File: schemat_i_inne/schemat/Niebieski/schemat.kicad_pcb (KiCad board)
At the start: 2 copper layers, 260.4 x 151.1 mm, 23 parts, among them J1 Hole1, J2 Hole2, J3 Hole3, J4 Hole4, J5 RJ45, SW1 SW_DIP_x01, SW2 Left, SW3 Up, SW4 Down, SW5 Right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

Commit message: Good footprints, before changes on PCB
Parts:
- added C3: 100N, Connector_PinHeader_2.54mm:PinHeader_1x02_P2.54mm_Vertical, F.Cu at (251.0, 105.7)
- added C4: 2.2uF, Connector_PinHeader_2.54mm:PinHeader_1x02_P2.54mm_Vertical, F.Cu at (281.6, 70.4)
- added R1: 4K7, Resistor_SMD:R_0805_2012Metric_Pad1.20x1.40mm_HandSolder, F.Cu at (255.7, 104.8)
- added R2: 1K, Resistor_SMD:R_0805_2012Metric_Pad1.20x1.40mm_HandSolder, F.Cu at (286.3, 72.5)
- added R3: 1K, Resistor_SMD:R_0805_2012Metric_Pad1.20x1.40mm_HandSolder, F.Cu at (281.7, 76.7)
- added R4: 1K, Resistor_SMD:R_0805_2012Metric_Pad1.20x1.40mm_HandSolder, F.Cu at (286.3, 69.5)
- added U4: LF33_TO252, Package_TO_SOT_SMD:TO-252-2, F.Cu at (285.4, 64.0)
- added U5: SN74LS07, Package_DIP:DIP-14_W7.62mm_LongPads, F.Cu at (298.2, 63.5)
- added U6: SD, Connector_Card:SD_Kyocera_145638009511859+, F.Cu at (263.5, 74.3)
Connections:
- C2 pad 1: VCC -> +5V
- J1 pad 1: Net-(J1-Pad1) -> unconnected-(J1-Pad1)
- J2 pad 1: Net-(J2-Pad1) -> unconnected-(J2-Pad1)
- J3 pad 1: Net-(J3-Pad1) -> unconnected-(J3-Pad1)
- J4 pad 1: Net-(J4-Pad1) -> unconnected-(J4-Pad1)
- J5 pad 1: VCC -> +5V
- J5 pad 3: Net-(J5-Pad3) -> unconnected-(J5-Pad3)
- J5 pad 6: Net-(J5-Pad6) -> /SCK
- J5 pad 7: Net-(J5-Pad7) -> /MISO
- J5 pad 8: Net-(J5-Pad8) -> /MOSI
- RV1 pad 3: VCC -> +5V
- U1 pad 1: Net-(J5-Pad8) -> /MOSI
- U1 pad 10: Net-(U1-Pad10) -> unconnected-(U1-Pad10)
- U1 pad 17: VCC -> +5V
- U1 pad 2: Net-(J5-Pad7) -> /MISO
- U1 pad 27: VCC -> +5V
- U1 pad 29: Net-(U1-Pad29) -> unconnected-(U1-Pad29)
- U1 pad 3: Net-(J5-Pad6) -> /SCK
- U1 pad 30: Net-(U1-Pad30) -> unconnected-(U1-Pad30)
- U1 pad 31: Net-(U1-Pad31) -> unconnected-(U1-Pad31)
- U1 pad 32: Net-(U1-Pad32) -> unconnected-(U1-Pad32)
- U1 pad 33: Net-(U1-Pad33) -> unconnected-(U1-Pad33)
- U1 pad 37: Net-(R1-Pad2) -> /CS
- U1 pad 38: VCC -> +5V
- U1 pad 40: Net-(U1-Pad40) -> unconnected-(U1-Pad40)
- U1 pad 5: VCC -> +5V
- U1 pad 9: Net-(U1-Pad9) -> unconnected-(U1-Pad9)
- U2 pad 3: VCC -> +5V
- U3 pad 17: VCC -> +5V
- U3 pad 19: VCC -> +5V
- U3 pad 4: VCC -> +5V
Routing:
- net +5V: track 0.00 -> 357.9 mm
- net VCC: track 357.9 -> 0.00 mm
- net Net-(J5-Pad7): track 146.5 -> 0.00 mm
- net /MISO: track 0.00 -> 146.5 mm
- net Net-(J5-Pad6): track 133.7 -> 0.00 mm
- net /SCK: track 0.00 -> 133.7 mm
- net Net-(J5-Pad8): track 132.3 -> 0.00 mm
- net /MOSI: track 0.00 -> 132.3 mm
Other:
- net class Default removed

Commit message: Wstepne sciezki z buforem
-> Dodano wstepne sciezki razem z buforem
-> Tam gdzie bylo to wymagane zmieniono warstwe
-> Dodano oporniki 0R we wlasciwych miejscach
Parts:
- added R5: 0R, Resistor_THT:R_Axial_DIN0207_L6.3mm_D2.5mm_P10.16mm_Horizontal, F.Cu at (252.0, 160.0)
- added R6: 0R, Resistor_THT:R_Axial_DIN0207_L6.3mm_D2.5mm_P10.16mm_Horizontal, F.Cu at (259.1, 144.8)
- C3, C4, U5: moved to B.Cu
- moved U4 88.5 mm to (285.0, 152.6), turned to 90 degrees
- moved C4 83.9 mm to (291.6, 153.7)
- moved U5 75.7 mm to (272.3, 134.6), turned to -90 degrees
- moved R2 62.2 mm to (266.7, 131.6), turned to -90 degrees
- moved R4 61.0 mm to (287.5, 130.6), turned to 180 degrees
- moved C3 57.1 mm to (278.9, 155.5)
- moved R3 54.2 mm to (269.2, 129.5), turned to -90 degrees
- moved R1 49.6 mm to (285.0, 144.8)
- moved U6 45.0 mm to (281.9, 115.3), turned to 180 degrees
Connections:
- C3 pad 1: +5V -> Net-(R1-Pad1)
- R1 pad 1: +5V -> Net-(R1-Pad1)
- U4 pad 1: +5V -> Net-(R1-Pad1)
- U5 pad 1: /CS -> Net-(U5-Pad1)
- U5 pad 14: +5V -> Net-(R1-Pad1)
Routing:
- net GND: track 858.1 -> 952.8 mm
- net +3V3: track 0.00 -> 71.9 mm
- net /MISO: track 146.5 -> 187.5 mm
- net /SCK: track 133.7 -> 169.1 mm
- net Net-(R1-Pad1): track 8.64 -> 41.7 mm
- net /MOSI: track 132.3 -> 164.2 mm
- net Net-(U5-Pad1): track 0.00 -> 29.2 mm
- net Net-(U5-Pad9): track 0.00 -> 25.0 mm
- net Net-(R3-Pad2): track 0.00 -> 19.2 mm
- net Net-(R2-Pad2): track 0.00 -> 16.1 mm
- net Net-(R4-Pad2): track 0.00 -> 11.0 mm
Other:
- board outline removed

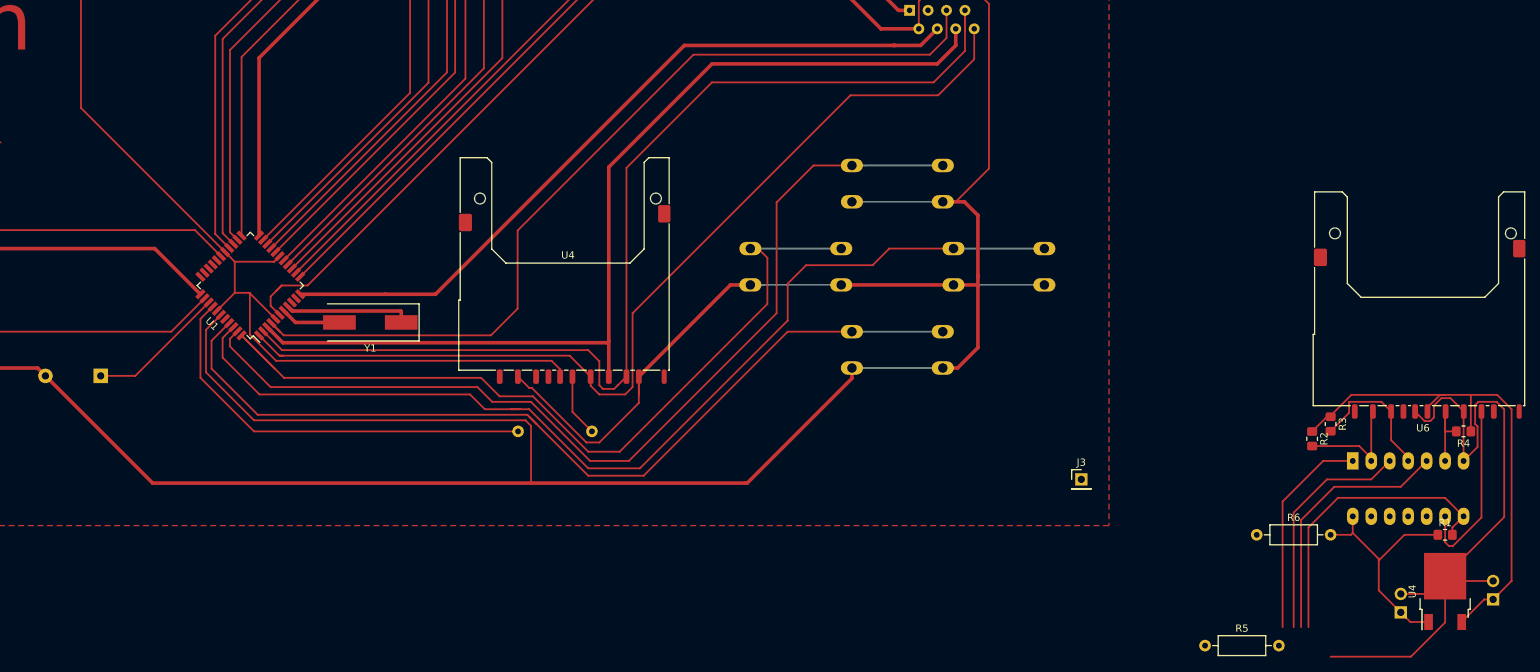
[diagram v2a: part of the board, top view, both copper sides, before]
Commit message: Awful but should work v2
-> Wszystko zostalo prowizorycznie podlaczone
-> uzyto 3 opornikow 0R
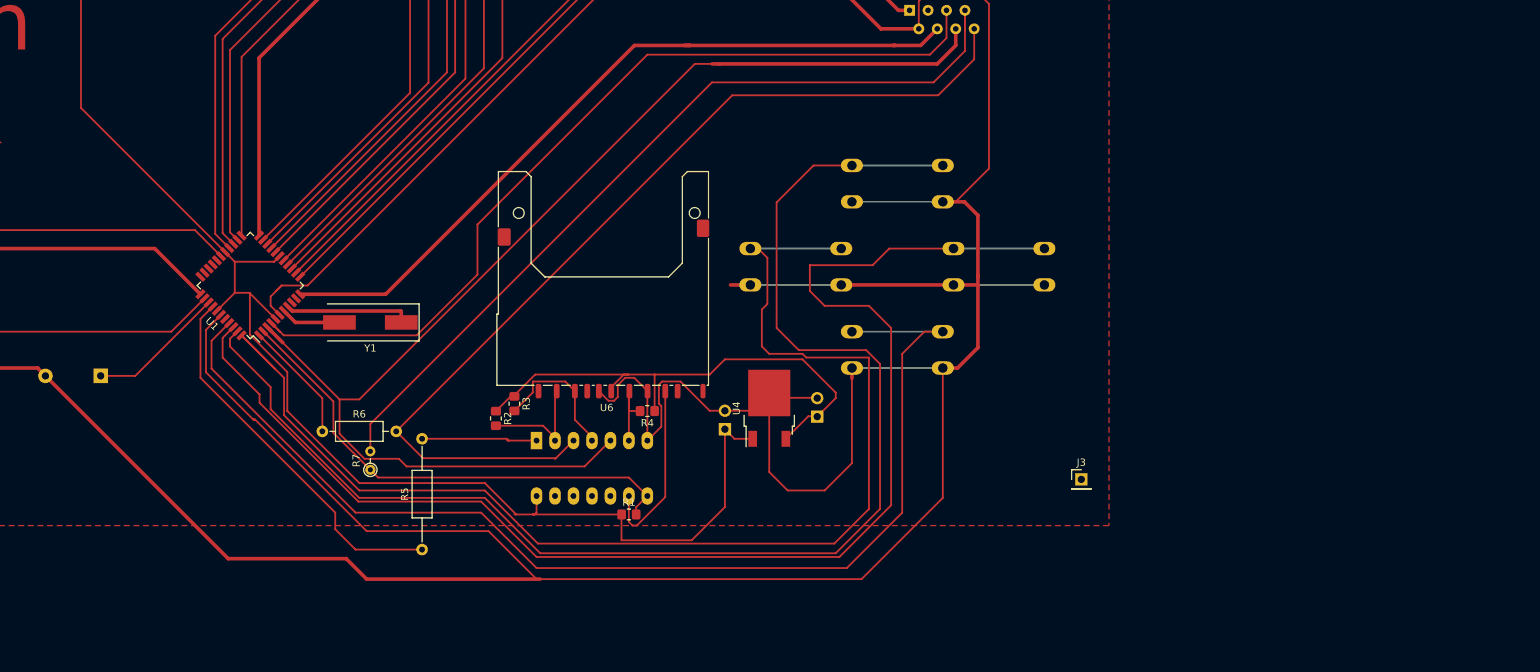
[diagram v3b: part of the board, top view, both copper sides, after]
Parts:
- removed the R1 at (167.6, 130.6)
- removed the U4 at (164.3, 115.8)
- added R7: 0R, Resistor_THT:R_Axial_DIN0204_L3.6mm_D1.6mm_P2.54mm_Vertical, F.Cu at (137.2, 135.8)
- R5: footprint Resistor_THT:R_Axial_DIN0207_L6.3mm_D2.5mm_P10.16mm_Horizontal -> Resistor_THT:R_Axial_DIN0207_L6.3mm_D2.5mm_P15.24mm_Horizontal
- moved R6 129.3 mm to (130.6, 130.6)
- moved R4 112.3 mm to (175.3, 127.8)
- moved R1 112.3 mm to (172.7, 142.0)
- moved R2 112.3 mm to (154.4, 128.8)
- moved R3 112.3 mm to (157.0, 126.7)
- moved U5 112.3 mm to (160.0, 131.8)
- moved U6 112.3 mm to (169.7, 112.5)
- moved R5 108.5 mm to (144.3, 146.8), turned to 90 degrees
- moved C3 96.3 mm to (185.9, 130.3)
- moved U4 96.3 mm to (192.0, 127.4)
- moved C4 96.3 mm to (198.6, 128.5)
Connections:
- C3 pad 1: Net-(R1-Pad1) -> +5V
- J5 pad 7: /MISO -> Net-(J5-Pad7)
- J5 pad 8: /MOSI -> Net-(U5-Pad3)
- R1 pad 1: Net-(R1-Pad1) -> +5V
- R6 pad 1: +5V -> /MOSI
- R6 pad 2: Net-(R1-Pad1) -> Net-(U5-Pad3)
- U4 pad 1: Net-(R1-Pad1) -> +5V
- U5 pad 14: Net-(R1-Pad1) -> +5V
- U5 pad 3: /MOSI -> Net-(U5-Pad3)
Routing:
- net /MOSI: track 164.2 -> 16.9 mm
- net Net-(U5-Pad3): track 0.00 -> 132.2 mm
- net /MISO: track 187.5 -> 67.9 mm
- net Net-(J5-Pad7): track 0.00 -> 115.5 mm
- net GND: track 952.8 -> 855.4 mm
- net Net-(SW2-Pad1): track 115.5 -> 173.7 mm
- net Net-(R1-Pad2): track 57.9 -> 0.00 mm
- net +5V: track 357.9 -> 414.7 mm
- net Net-(SW3-Pad1): track 132.8 -> 186.5 mm
- net /CS: track 0.00 -> 52.8 mm
- net Net-(SW5-Pad1): track 140.6 -> 186.1 mm
- net Net-(R1-Pad1): track 41.7 -> 0.00 mm
- net Net-(SW4-Pad1): track 123.6 -> 158.0 mm
- net Net-(R5-Pad2): track 29.2 -> 16.1 mm
- net Net-(J5-Pad5): track 122.6 -> 120.4 mm
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
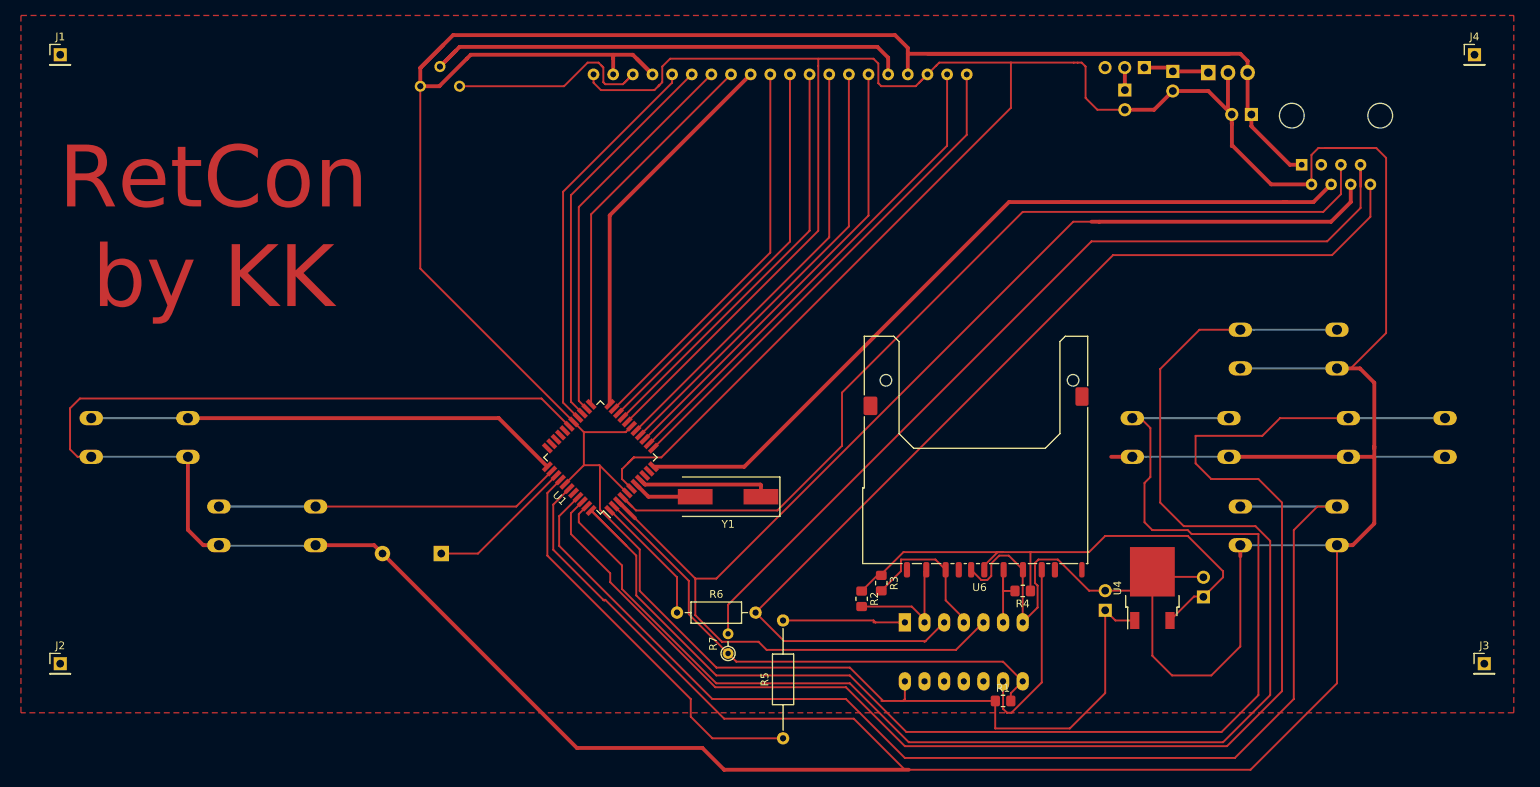
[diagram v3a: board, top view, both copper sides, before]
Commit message: Not all connections, but better positions
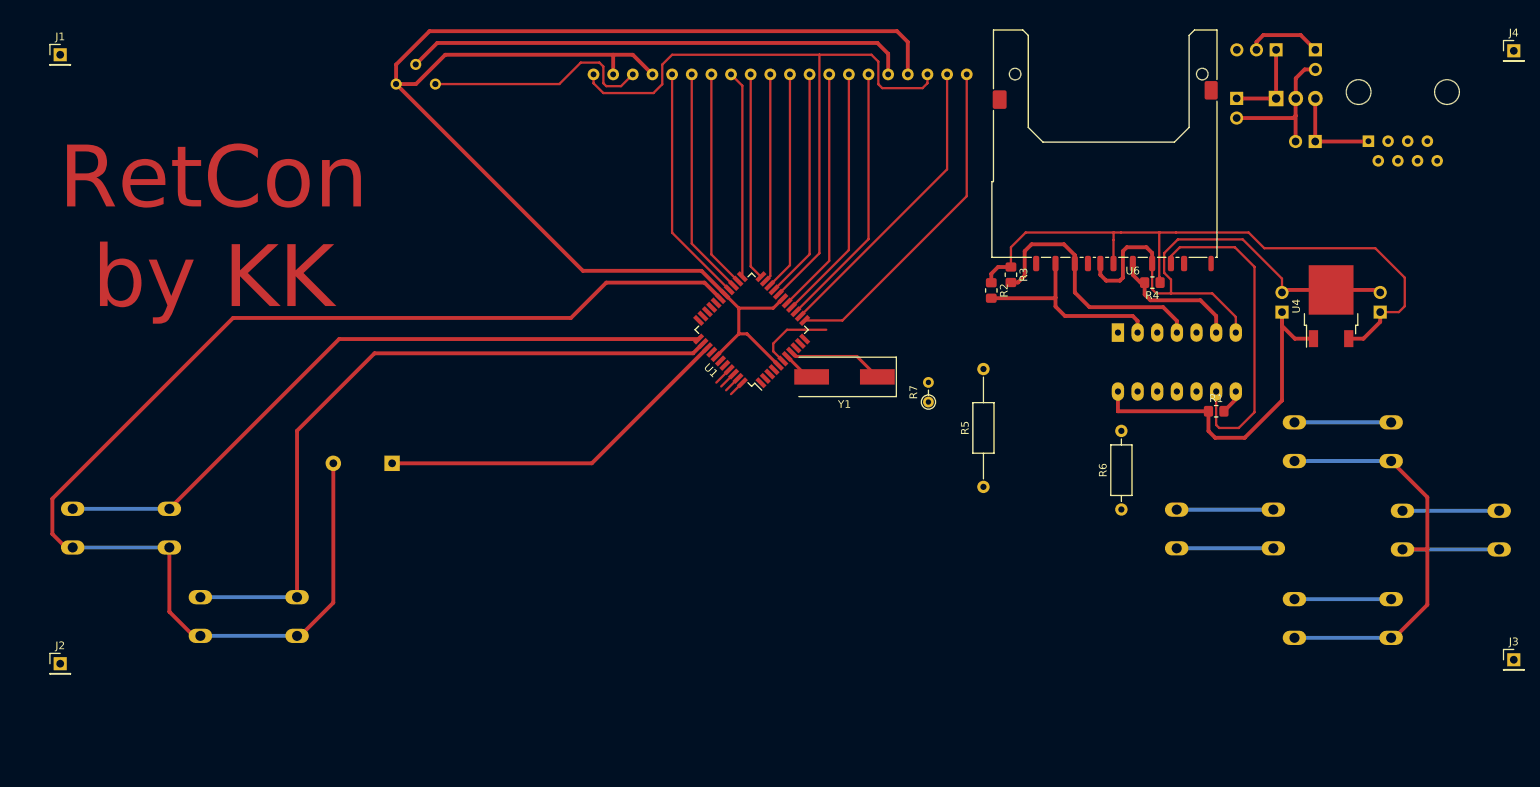
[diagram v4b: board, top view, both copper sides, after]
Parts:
- moved R6 59.0 mm to (188.0, 117.2), turned to 90 degrees
- moved U5 46.5 mm to (187.6, 94.3)
- moved R1 46.5 mm to (200.3, 104.5)
- moved C3 44.8 mm to (208.8, 91.7)
- moved C4 43.3 mm to (221.5, 91.7)
- moved R4 43.3 mm to (192.0, 87.9)
- moved R3 43.3 mm to (173.7, 86.9)
- moved R2 43.3 mm to (171.2, 88.9)
- moved U4 43.2 mm to (215.1, 90.9)
- moved U6 43.0 mm to (186.4, 72.9)
- moved R5 41.6 mm to (170.2, 114.3)
- moved R7 41.6 mm to (163.1, 103.3)
- moved U1 25.6 mm to (140.2, 94.0)
- moved BT1 25.2 mm to (213.1, 57.8)
- moved Y1 21.6 mm to (152.2, 100.1)
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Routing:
- net GND: track 855.4 -> 435.8 mm
- net Net-(SW3-Pad1): track 186.5 -> 14.7 mm
- net Net-(SW5-Pad1): track 186.1 -> 14.8 mm
- net /SCK: track 170.6 -> 0.00 mm
- net +5V: track 414.7 -> 249.5 mm
- net Net-(SW2-Pad1): track 173.7 -> 14.6 mm
- net Net-(SW4-Pad1): track 158.0 -> 14.9 mm
- net Net-(J5-Pad4): track 132.5 -> 0.00 mm
- net Net-(U5-Pad3): track 132.2 -> 0.00 mm
- net Net-(J5-Pad5): track 120.4 -> 0.00 mm
- net Net-(J5-Pad7): track 115.5 -> 0.00 mm
- net /MISO: track 67.9 -> 3.19 mm
- net /CS: track 52.8 -> 0.00 mm
- net Net-(SW6-Pad1): track 44.9 -> 91.2 mm
- net Net-(SW7-Pad1): track 61.6 -> 90.0 mm
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- removed copper zone on F.Cu, net GND

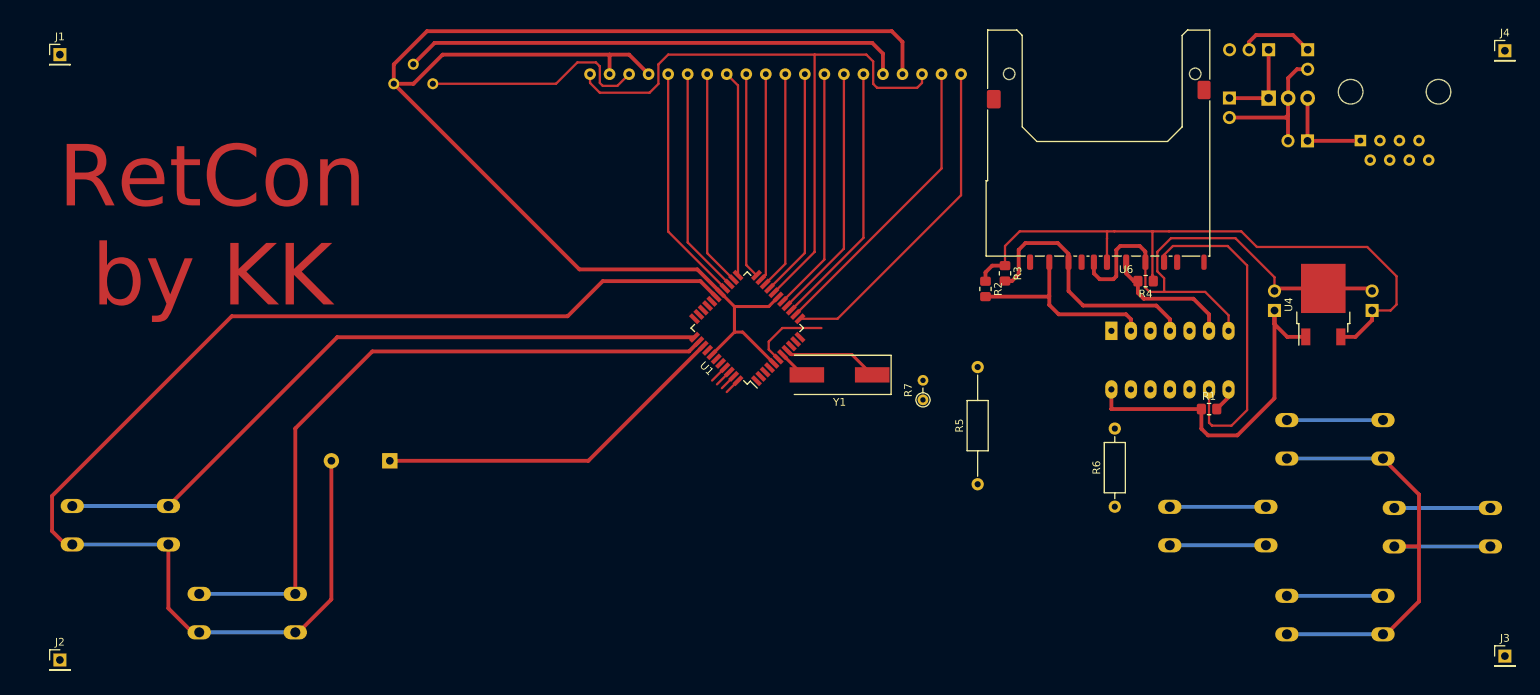
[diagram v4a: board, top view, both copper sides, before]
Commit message: Ukonczone polaczenia
-> skonczone polaczenia poprawionego schematu
po przeniesieniu karty
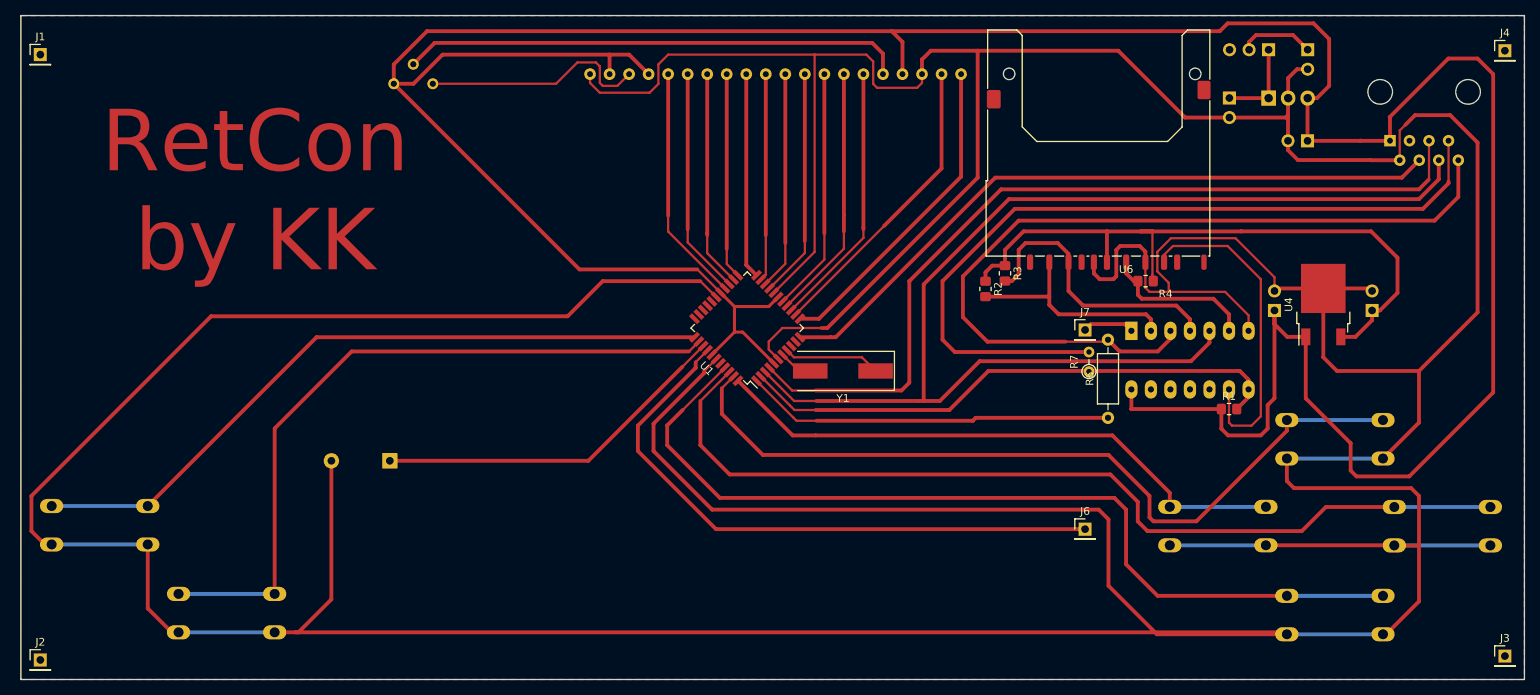
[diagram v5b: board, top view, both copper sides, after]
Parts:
- removed R5: 0R, Resistor_THT:R_Axial_DIN0207_L6.3mm_D2.5mm_P15.24mm_Horizontal
- added J6: Conn_01x01_Male, Connector_PinHeader_2.54mm:PinHeader_1x01_P2.54mm_Vertical, F.Cu at (184.2, 120.1)
- added J7: Conn_01x01_Male, Connector_PinHeader_2.54mm:PinHeader_1x01_P2.54mm_Vertical, F.Cu at (184.2, 94.2)
- moved R7 21.9 mm to (184.7, 99.6)
- moved R6 11.6 mm to (187.1, 105.7)
- moved J5 3.85 mm to (223.8, 69.6)
- moved SW6 2.68 mm to (78.7, 128.6)
- moved SW7 2.68 mm to (62.2, 117.1)
- moved R1 2.60 mm to (202.9, 104.5)
- moved U5 2.60 mm to (190.2, 94.3)
- moved J1 2.54 mm to (48.3, 58.4)
- moved J2 2.54 mm to (48.3, 137.2)
- moved Y1 0.67 mm to (152.7, 99.6)
- moved SW5 0.13 mm to (236.9, 117.3)
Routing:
- net GND: track 435.8 -> 908.4 mm
- net +5V: track 249.5 -> 425.4 mm
- net /SCK: track 0.00 -> 154.3 mm
- net Net-(J5-Pad5): track 0.00 -> 111.2 mm
- net Net-(J5-Pad8): track 0.00 -> 109.6 mm
- net Net-(SW5-Pad1): track 14.8 -> 121.2 mm
- net Net-(SW4-Pad1): track 14.9 -> 118.9 mm
- net Net-(J5-Pad7): track 0.00 -> 104.0 mm
- net Net-(SW3-Pad1): track 14.7 -> 105.2 mm
- net Net-(J5-Pad4): track 0.00 -> 90.1 mm
- net /CS: track 0.00 -> 79.2 mm
- net /MISO: track 3.19 -> 72.3 mm
- net Net-(SW2-Pad1): track 14.6 -> 76.5 mm
- net /MOSI: track 0.00 -> 48.0 mm
- net Net-(U5-Pad1): track 0.00 -> 6.70 mm
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- added copper zone on F.Cu, net GND
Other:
- board outline added: 195.6 x 86.4 mm
- board text added: "optional- if needed"
